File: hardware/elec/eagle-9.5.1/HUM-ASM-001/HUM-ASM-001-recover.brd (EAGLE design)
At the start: 99.1 x 99.1 mm, 61 parts, among them J1 B2B-XH-AM(LF)(SN), J2 75869-131LF, J22 75869-131LF, J23 75869-131LF, K1 7-1393239-7, K2 7-1393239-7, Q1 IRLB8721PBF, Q2 IRLB8721PBF, U1 MCP23017-E/SP

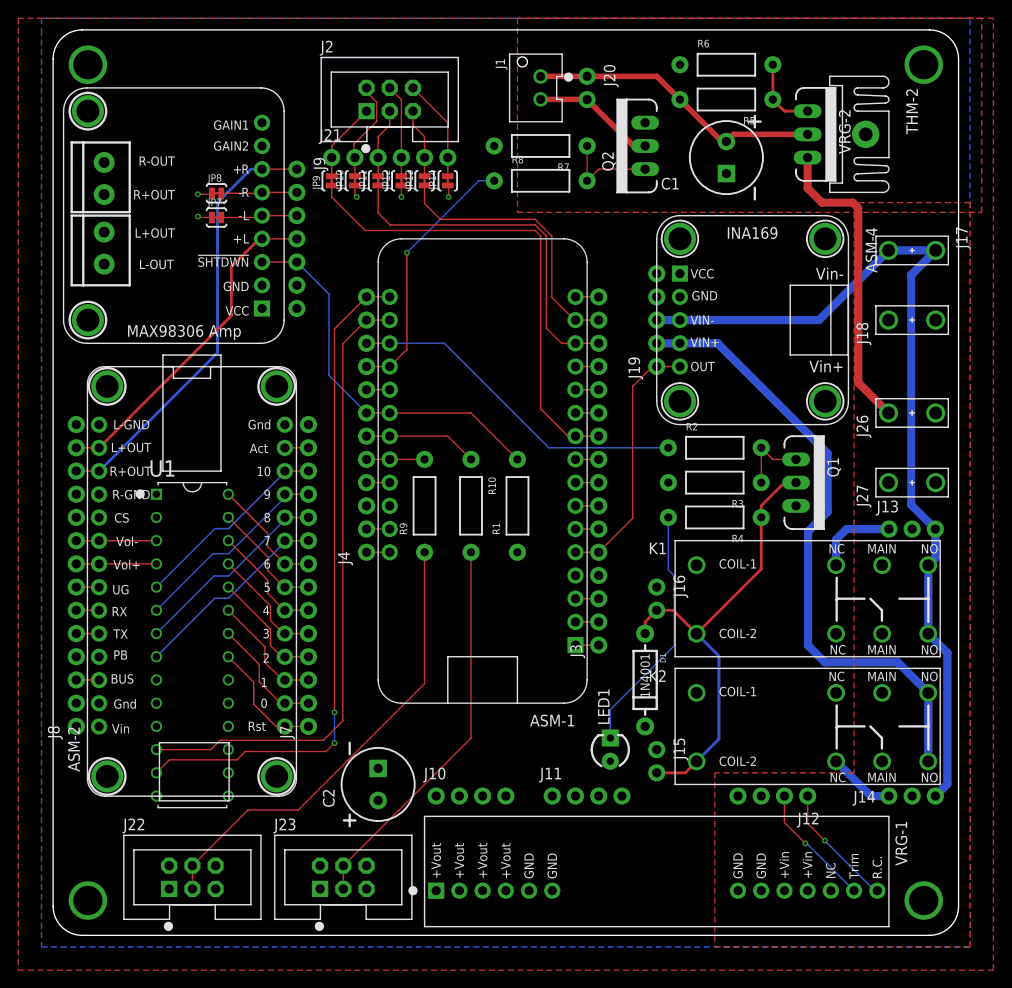
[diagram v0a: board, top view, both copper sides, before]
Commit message: * Fixed crash / recovery inconsistency * Pre silk screen clean up
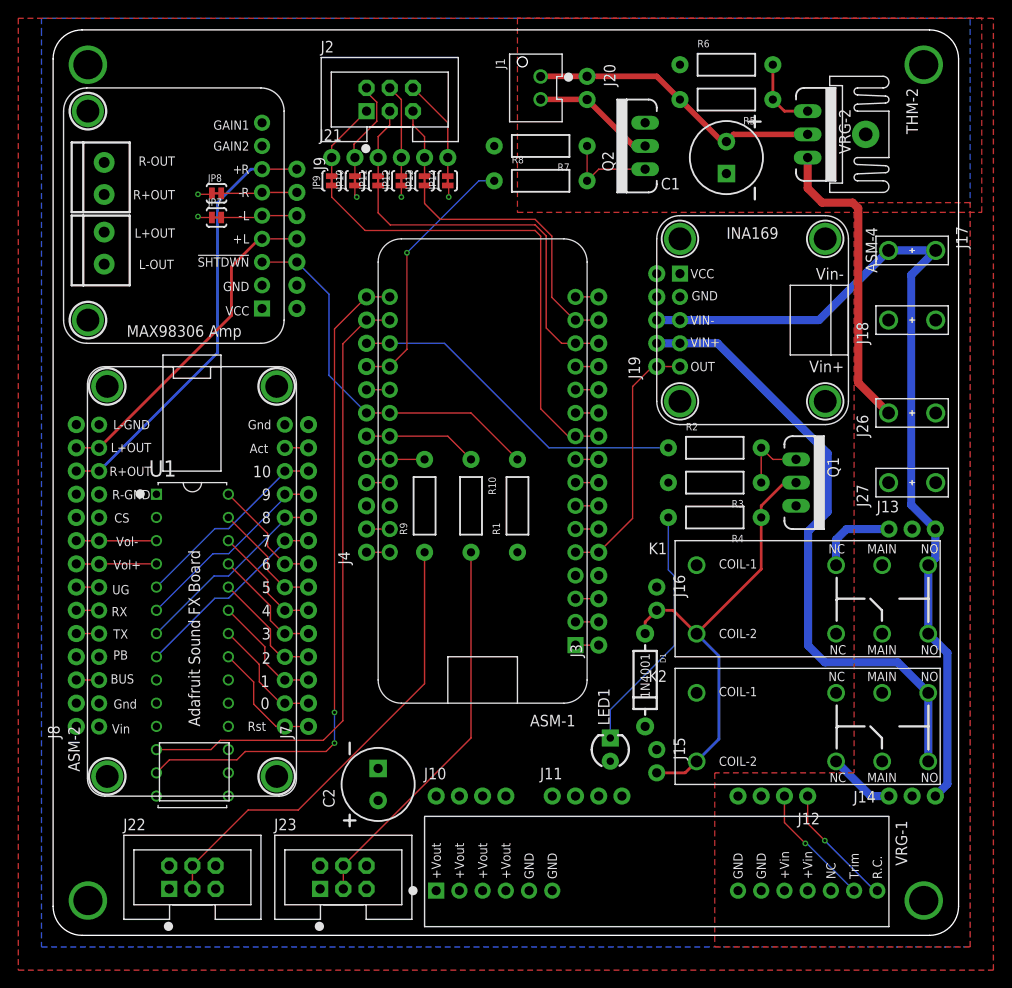
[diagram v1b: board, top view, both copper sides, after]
